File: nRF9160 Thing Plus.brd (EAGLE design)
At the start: 58.4 x 22.9 mm, 124 parts, among them J1 USB Female C, J10 QWIIC_RIGHT_ANGLE, J2 CON-HEADER-1X12-MALE-PIN, J3 CON-HEADER-1X16-MALE-PIN, J4 CON-1909763-1, J6 CON-S2B-PH-SM4-TB(LF)(SN), J7 CON-1909763-1, J9 CON-0002, P1 CON-SIM-SF72S006VBAR2500, Q1 MOSFET-P-SC89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

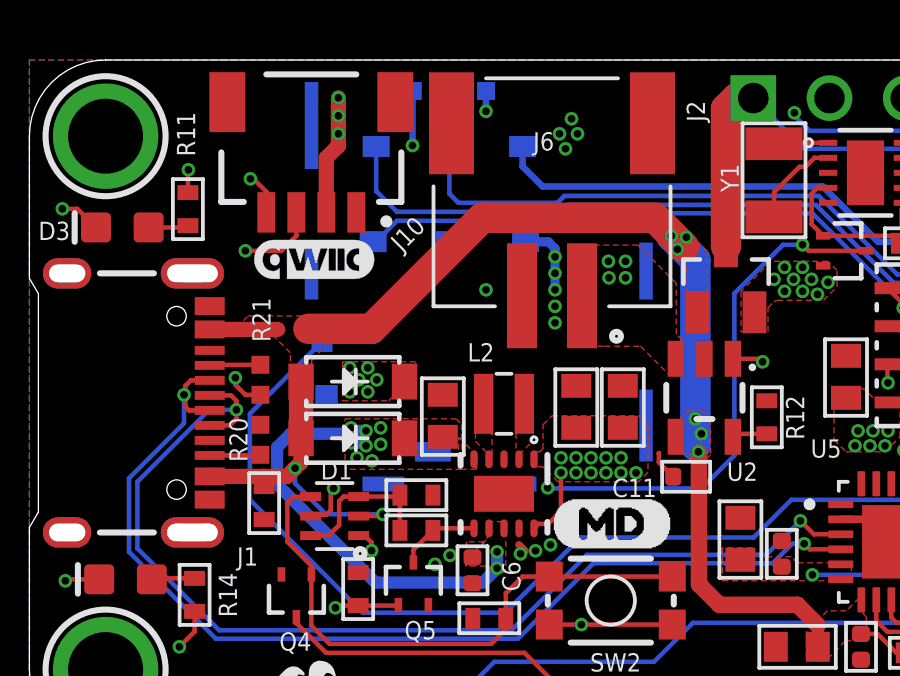
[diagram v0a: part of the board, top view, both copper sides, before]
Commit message: Changed C9 to match other 4.7u caps. Update D5/D6 to BAT60A Updated J5 to match Sparkfun's JST connector
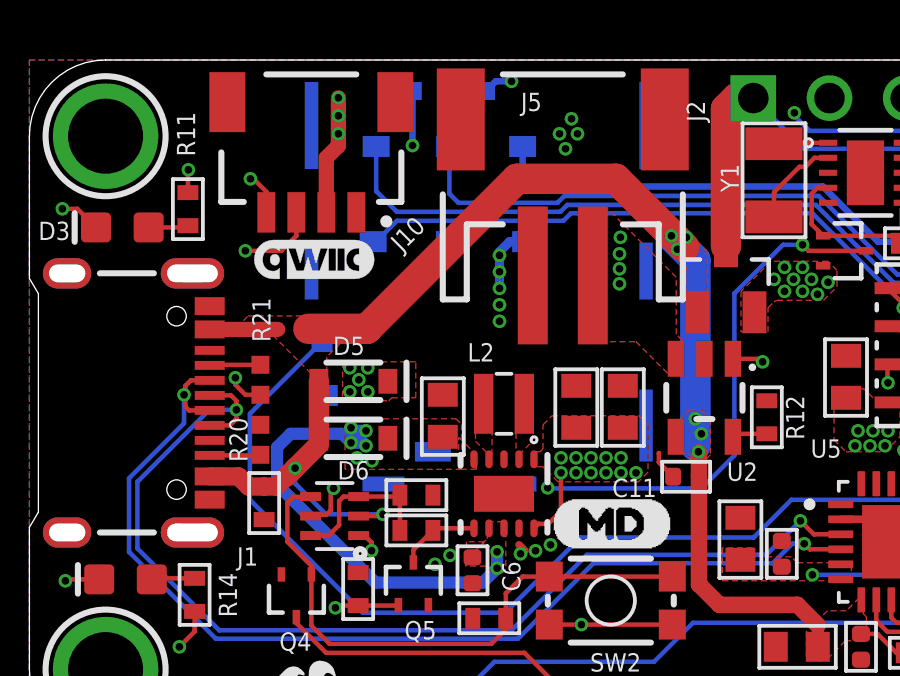
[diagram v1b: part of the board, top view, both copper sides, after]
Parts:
- removed D1, D2: DIO-SCHOTTKY-3A-01, wolff-den:SOD123
- removed J6: CON-S2B-PH-SM4-TB(LF)(SN), wolff-den:JST_S2B-PH-SM4-TB(LF)(SN)
- added D5, D6: 3A/10V/280mV, SparkFun-DiscreteSemi:SOD-323
- added J5: (no value), SparkFun-Connectors:JST-2-SMD
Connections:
- net GND: now also J5.1; no longer J6.2, J6.S1, J6.S2
- net VBAT: now also J5.2; no longer J6.1
- net VBUS: now also D5.A, D6.A; no longer D1.2, D2.2
- net VCC_5V0: now also D5.C; no longer D2.1
- net VSYS: now also D6.C; no longer D1.1
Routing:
- net VBUS: track 47.8 -> 49.1 mm
- net VBAT: track 25.2 -> 26.3 mm
- net GND: vias 66 -> 65
- net VSYS: vias 22 -> 20
- net VCC_5V0: vias 6 -> 5

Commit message: Modifying mode pin to be connected directly to the MD button. (useful for external wakeup)
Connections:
- removed net MODE: Q4.1, R13.2, SW2.3, SW2.4, U9.4
- new net MODE/WAKE: J3.3, Q4.1, R13.2, SW2.3, SW2.4, U9.4
- net P0.12/MD: no longer J3.3
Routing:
- net MODE/WAKE: track 0.00 -> 23.8 mm
- net MODE: track 19.5 -> 0.00 mm
- net P0.12/MD: track 30.6 -> 29.4 mm, vias 1 -> 2

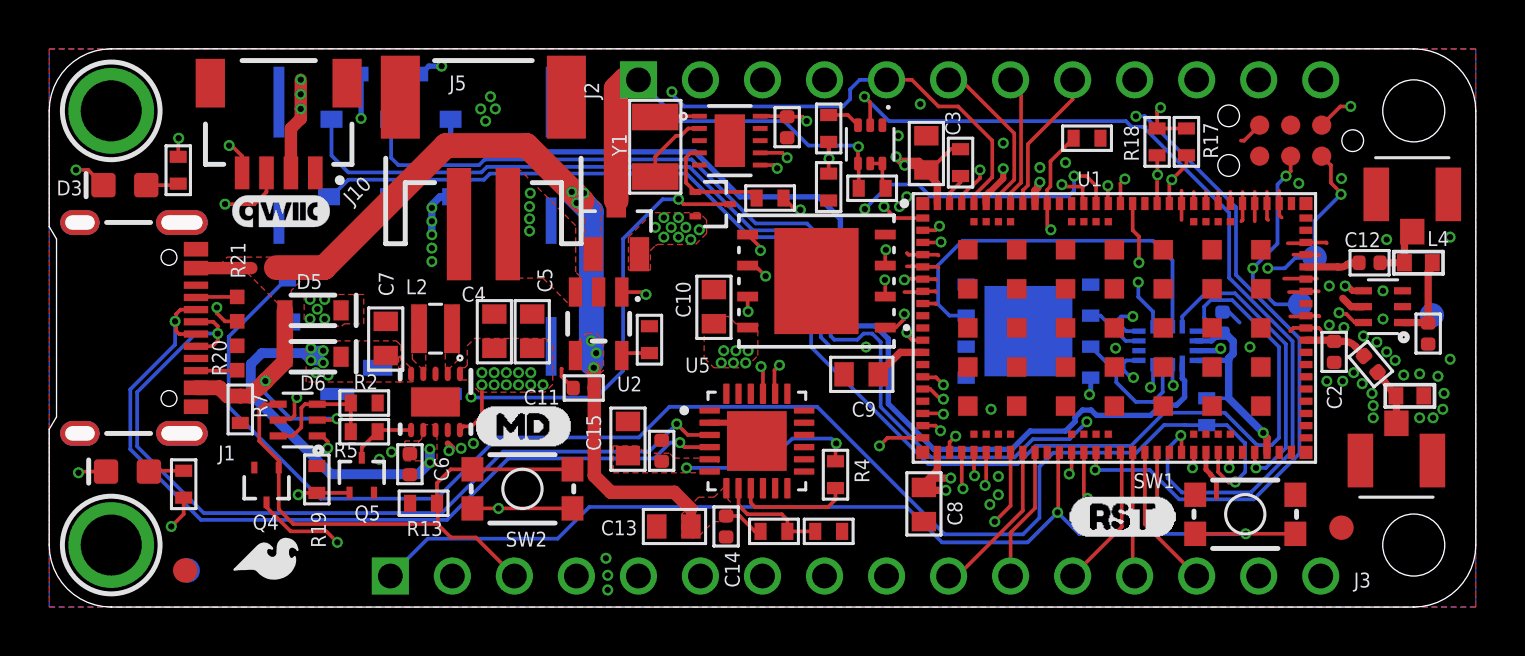
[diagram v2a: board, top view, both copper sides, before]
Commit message: Adding LIS2DH12TR and supporting components. Adding jumpers for D2 (Accel int) and also PS_EN
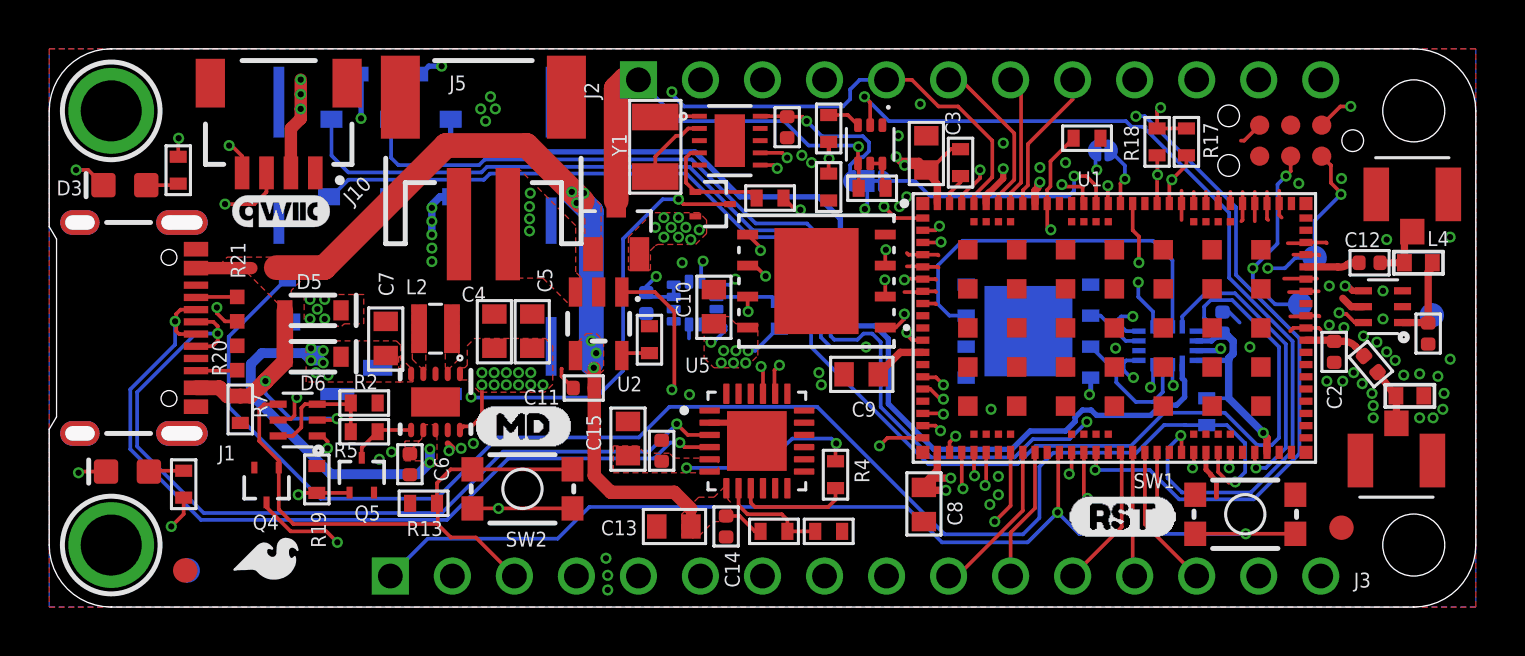
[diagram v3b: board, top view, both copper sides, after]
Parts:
- added C20: 0.1u, wolff-den:CAPC1005X55N
- added JMP1: JUMPER-NC, wolff-den:JUMPER-ROUND-NC
- added JMP2: JUMPER-3/1, wolff-den:JUMPER-ROUND-3-NO-R
- added R23: 100k, wolff-den:R0402-M
- added U12: IC-LIS2DH12TR, wolff-den:PQFN50P200X200100-12N
- U$8: device buzzard_labels (2):NC13 -> buzzard_labels-18:PS_EN0
- moved U$1 2.28 mm to (26.0, 6.90)
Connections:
- new net N$11: R23.1, U12.2
- new net N$12: JMP1.P$1, U12.12
- new net NRF_PS_EN_JMP: JMP2.P$2, U9.1
- net +3V3: now also C20.1, R23.2, U12.10, U12.9
- net GND: now also C20.2, U12.3, U12.5, U12.6, U12.7, U12.8
- net P0.26/SDA: now also U12.4
- net P0.27/SCL: now also U12.1
- net P0.29/D2: now also JMP1.P$2
- net P0.31/NRF_PS_EN: now also J3.16, JMP2.P$3; no longer U9.1
- net VSYS: now also JMP2.P$1
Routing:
- net NRF_PS_EN_JMP: track 0.00 -> 29.6 mm, vias 0 -> 2
- net N$12: track 0.00 -> 28.6 mm, vias 0 -> 2
- net P0.26/SDA: track 57.2 -> 66.9 mm, vias 3 -> 4
- net P0.27/SCL: track 51.7 -> 58.3 mm, vias 3 -> 4
- net VSYS: track 55.3 -> 60.2 mm
- net P0.31/NRF_PS_EN: track 40.0 -> 35.1 mm, vias 3 -> 1
- net +3V3: track 23.7 -> 27.9 mm, vias 30 -> 31
- net CHRG: track 31.1 -> 34.1 mm
- net N$11: track 0.00 -> 2.66 mm
- net P0.29/D2: track 6.36 -> 7.78 mm
- net GND: track 42.1 -> 42.7 mm, vias 65 -> 71
